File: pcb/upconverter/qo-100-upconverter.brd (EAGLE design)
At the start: 100 x 70 mm, 222 parts, among them CON1 3P-SH-SIDE, CON2 2EDG-2P-5MM-H, U1 EFM32TG11B120F128GM32, U10 LTC5597, U11 2450BP15E0100, U12 DC2337J5010AHF, U13 MCP6V31, U14 SKY66292-11, U15 F1958NBGK, U16 MCP9802-A0, U17 MCP1700-330, U18 LT8636, U19 MCP3421-A0, U2 DSB321SDA, U20 MCP6C02-020, U21 ADP7142AUJZ-3.3, U22 ADP7142AUJZ-3.3, U23 ADP7142AUJZ-3.3, U24 ADM7171ACPZ-5.0, U25 ADM7172ACPZ-5.0, U3 ADF4351, U4 F1958NBGK, U5 MAX2671, U6 2450BP15E0100, U7 F1958NBGK, U8 ADL5601, U9 F1490NLGA

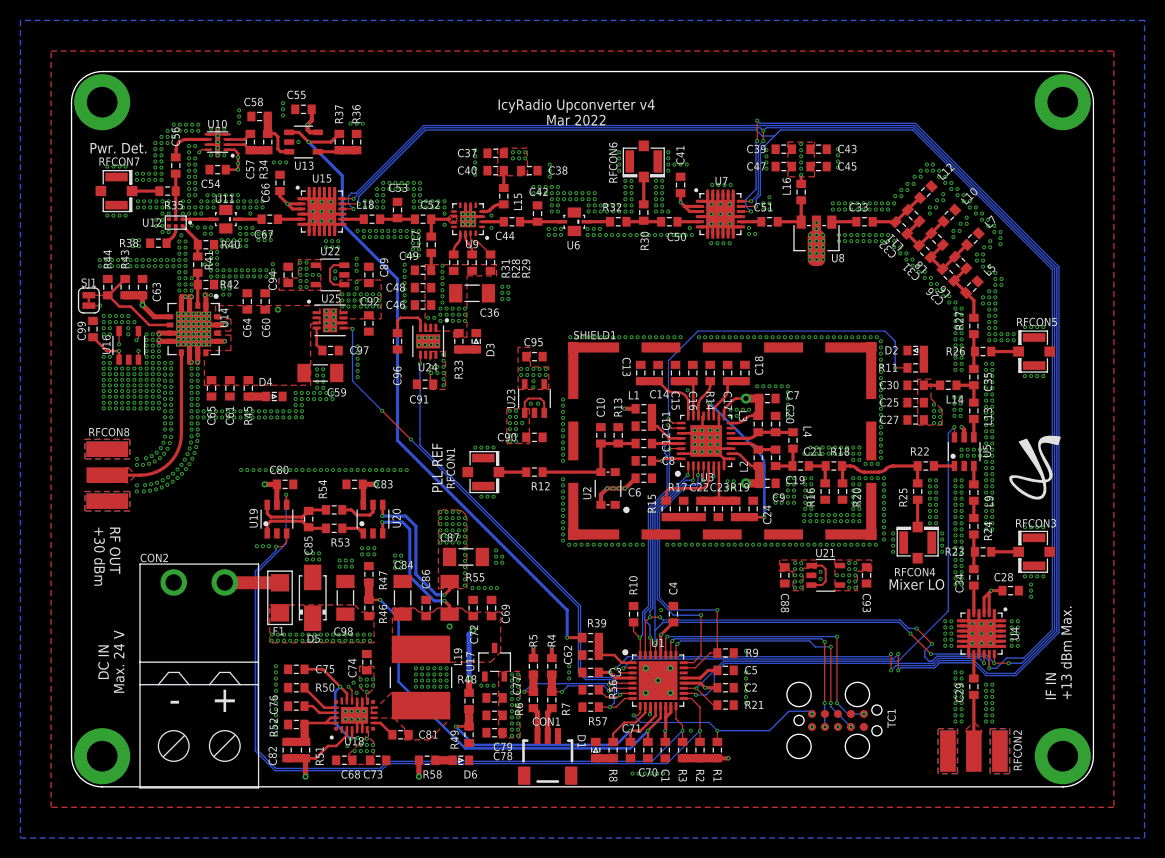
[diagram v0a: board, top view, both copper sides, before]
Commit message: Add RF switch
Signed-off-by: João Silva <jgc3silva@gmail.com>
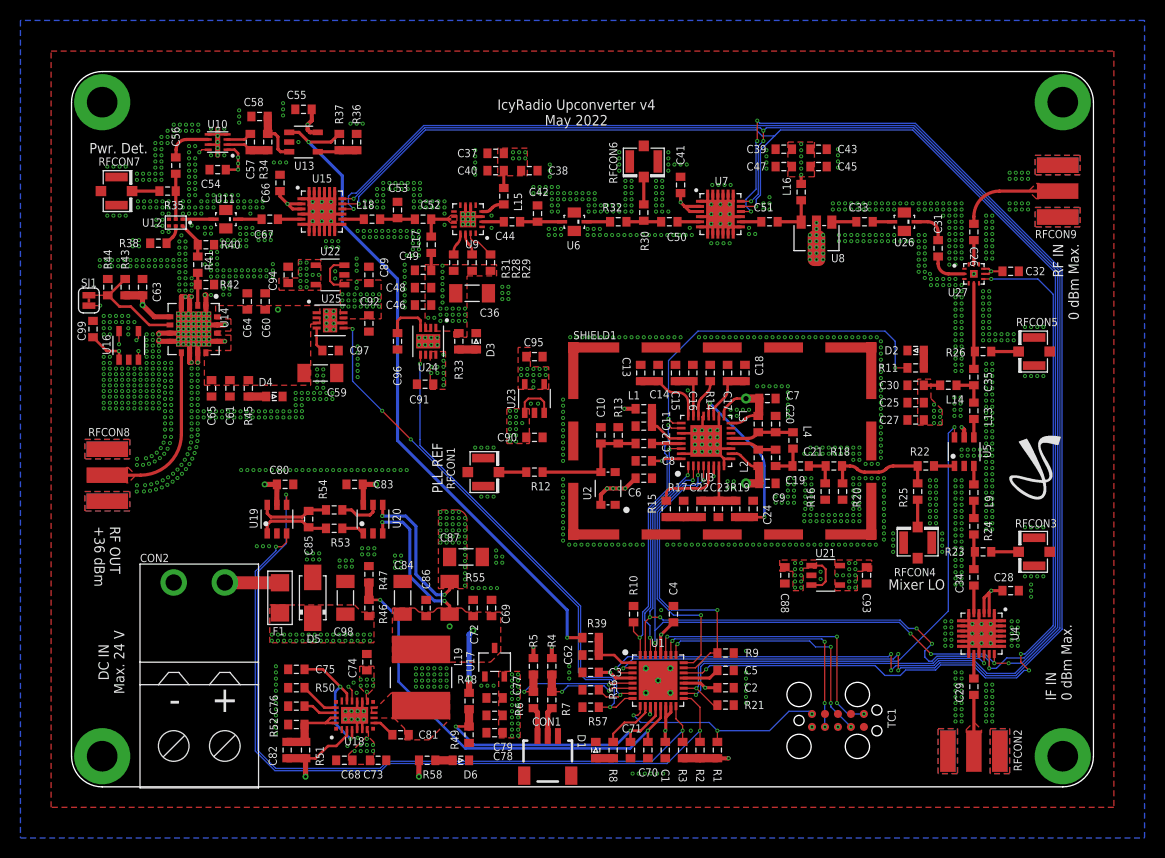
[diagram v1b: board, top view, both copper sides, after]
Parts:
- removed L10: 1.8pF, Inductor:IND0603
- removed L11, L8: 0 Ohms, Inductor:IND0603
- removed L12: 2.2pF, Inductor:IND0603
- removed L5, L6: 5.1nH, Inductor:IND0603
- removed L7: 3.3nH, Inductor:IND0603
- removed R27: 0 Ohms, Resistor:RES0603
- added RFCON9: RFCON-SMA-EDGE, RF Connector:SMA-EDGE
- added U26: 2450BP15E0100, Generic Filter:2450BP15E0100
- added U27: JSW2-63DR+, Mini Circuits:MT1818
- C26: value 1.2pF -> 12pF
- C31: value DNP -> 12pF
- C32: value DNP -> 100nF
- moved C32 11.5 mm to (91.9, 50.5), turned to 0 degrees
- moved C26 4.89 mm to (88.3, 54.3), turned to 270 degrees
- moved C31 1.33 mm to (84.8, 52.7), turned to 90 degrees
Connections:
- net RF_LOL_FLT_ACC renamed RF_FLT_ACC
- removed net 3V3_IF_ATT_MIXER_CLEAN: C25.1, C27.1, C28.1, C30.1, C93.1, L14.2, U21.4, U21.5, U4.2, U4.3, U5.5
- removed net MIXER_OUT_ACC_PROBE: C35.2, R26.1, R27.2
- removed net N$32: C26.2, C31.1, L6.2, L7.2, L8.1
- removed net N$33: C31.2, C32.1, L10.2, L11.1, L8.2
- removed net N$34: C32.2, C33.1, L11.2, L12.2
- removed net RF_ACC: C26.1, L5.2, L6.1, R27.1
- new net 3V3_IF_ATT_MIXER_SW_CLEAN: C25.1, C27.1, C28.1, C30.1, C32.1, C93.1, L14.2, U21.4, U21.5, U27.8, U27.9, U4.2, U4.3, U5.5
- new net MIXER_OUT_ACC: C35.2, R26.1, U27.5
- new net RF_IN_ACC: C26.2, U27.11
- new net RF_IN_DCC: C26.1, RFCON9.SIG
- new net RF_SEL_ACC: C31.2, U26.4
- new net RF_SEL_DCC: C31.1, U27.2
- new net RF_SEL_FILT_DCC: C33.1, U26.2
- new net RF_SW_CTL: U1.22, U27.7
- net GND: now also C32.2, RFCON9.GND@0, RFCON9.GND@1, RFCON9.GND@2, RFCON9.GND@3, U26.1, U26.3, U27.1, U27.10, U27.12, U27.17, U27.3, U27.4, U27.6; no longer L10.1, L12.1, L5.1, L7.1
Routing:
- net RF_SW_CTL: track 0.00 -> 81.9 mm, vias 0 -> 4
- net 3V3_IF_ATT_MIXER_SW_CLEAN: track 0.00 -> 11.4 mm, vias 0 -> 22
- net RF_IN_DCC: track 0.00 -> 9.94 mm
- net MIXER_OUT_ACC: track 0.00 -> 8.65 mm
- net 3V3_IF_ATT_MIXER_CLEAN: track 8.58 -> 0.00 mm, vias 21 -> 0
- net N$32: track 6.73 -> 0.00 mm
- net N$33: track 6.73 -> 0.00 mm
- net RF_ACC: track 6.22 -> 0.00 mm
- net N$34: track 5.63 -> 0.00 mm
- net RF_SEL_DCC: track 0.00 -> 3.69 mm
- net MIXER_OUT_ACC_PROBE: track 3.50 -> 0.00 mm
- net RF_SEL_ACC: track 0.00 -> 3.31 mm
- net RF_IN_ACC: track 0.00 -> 2.38 mm
- net RF_SEL_FILT_DCC: track 0.00 -> 1.90 mm
- net !MIXER_SHDN: track 51.2 -> 52.4 mm
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- added copper zone on layer 1, net 3V3_IF_ATT_MIXER_SW_CLEAN
- added copper zone on layer 15, net 3V3_IF_ATT_MIXER_SW_CLEAN
- added copper zone on layer 1, net RF_IN_DCC
- removed copper zone on layer 1, net 3V3_IF_ATT_MIXER_CLEAN
- removed copper zone on layer 15, net 3V3_IF_ATT_MIXER_CLEAN
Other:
- board text added: "IF IN 0 dBm Max."
- board text added: "IcyRadio Upconverter v4 May 2022"
- board text added: "RF IN 0 dBm Max."
- board text added: "RF OUT +36 dBm"
- board text removed: "IF IN +13 dBm Max."
- board text removed: "IcyRadio Upconverter v4 Mar 2022"
- board text removed: "RF OUT +30 dBm"

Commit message: Add Mixer and RF Switch indicator LEDs Slightly raise switched 5V0 rail voltage to account for larger current drawn from higher power last stage Remove dedicated ADC for current sampling Added PCB preview pictures Added schematic PDF
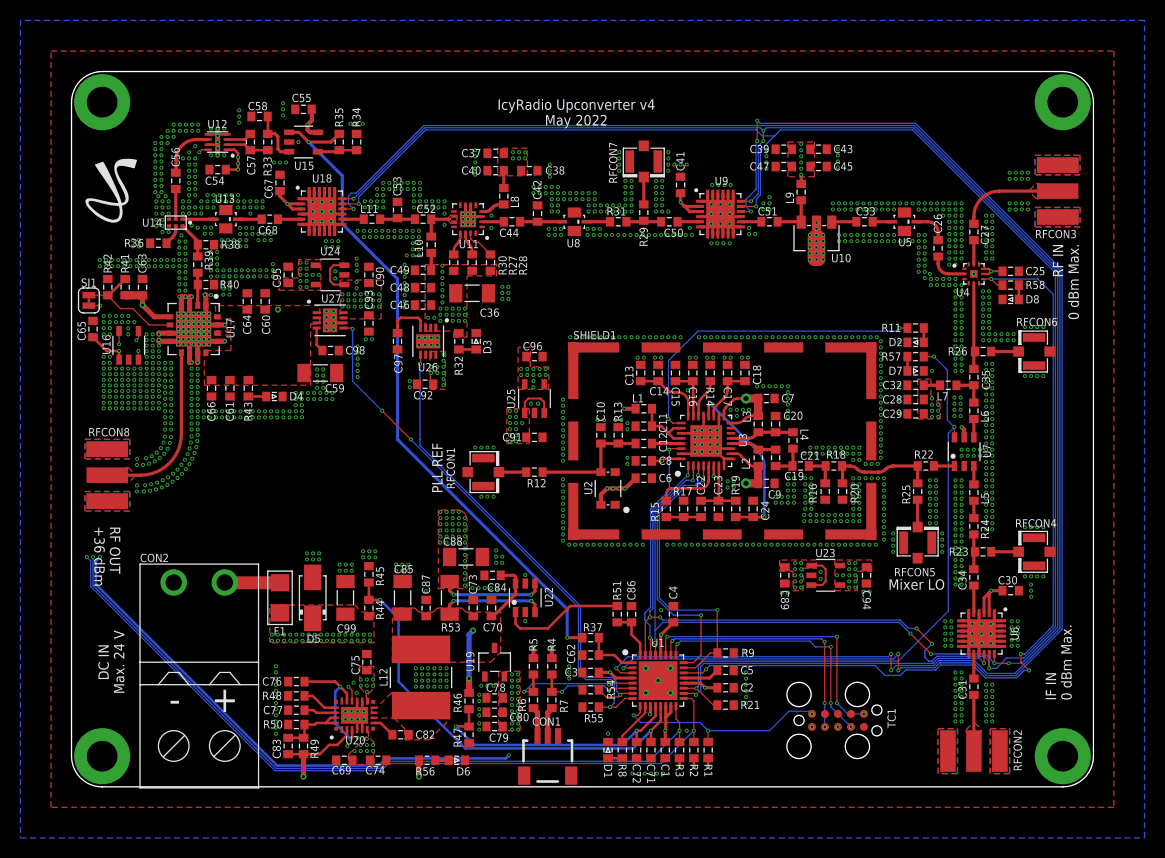
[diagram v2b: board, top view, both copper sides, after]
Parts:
- removed C81: 100nF, Capacitor:CAP0603
- removed L16: 470nH, Inductor:IND0603
- removed R10: 100K Ohms, Resistor:RES0603
- removed R52: 221K Ohms, Resistor:RES0603
- removed RFCON9: RFCON-SMA-EDGE, RF Connector:SMA-EDGE
- removed U21: ADP7142AUJZ-3.3, Analog Devices:SOT23-5
- added D7, D8: LED0603, LED:0603
- added L5: 18nH, Inductor:IND0603
- added R27: 1K Ohms, Resistor:RES0603
- C25: value 1uF -> 100nF
- C26, C33: value 12pF -> 15pF
- C27: value 100nF -> 15pF
- C28: value 100nF -> 1uF
- C29: value 100pF -> 100nF
- C30: value 47pF -> 100nF
- C31: value 12pF -> 100pF
- C32: value 100nF -> 47pF
- C65: value 10nF -> 100nF
- C66, C77: value 100nF -> 10nF
- C67: value 15pF -> 100nF
- C68: value 4.7uF -> 15pF
- C69: value 100nF -> 4.7uF
- C70: value 470pF -> 100nF
- C72: value 4.7uF -> 470pF
- C73: value 1uF -> 4.7uF
- C76: value 10nF -> 1uF
- C78: value 10uF -> 100nF
- C80: value 100nF -> 10uF
- C82: value 10pF -> 100nF
- C83: value 1uF -> 10pF
- C84: value 100uF -> 1uF; device Capacitor:CAP1206 -> Capacitor:CAP0603
- C85: value 100nF -> 100uF; device Capacitor:CAP0603 -> Capacitor:CAP1206
- C87: value 22uF -> 100nF; device Capacitor:CAP1206 -> Capacitor:CAP0603
- C88: value 1uF -> 22uF; device Capacitor:CAP0603 -> Capacitor:CAP1206
- C93: value 10uF -> 1uF
- C96: value 1nF -> 10uF
- C98: value 10uF -> 1nF; device Capacitor:CAP1206 -> Capacitor:CAP0603
- C99: value 100nF -> 10uF; device Capacitor:CAP0603 -> Capacitor:CAP1206
- L9: value 18nH -> 470nH
- R28: value 1K Ohms -> DNP
- R30: value DNP -> 1.5K Ohms
- R31: value 1.5K Ohms -> 0 Ohms
- R32: value 0 Ohms -> 510 Ohms
- R33: value 510 Ohms -> 0 Ohms
- R34: value 0 Ohms -> 1K Ohms
- R35: value DNP -> 2K Ohms
- R36: value 1K Ohms -> 49.9 Ohms
- R37: value 2K Ohms -> 100 Ohms
- R38: value 49.9 Ohms -> 96.1 Ohms
- R39: value 100 Ohms -> 71.5 Ohms
- R41: value 71.5 Ohms -> 10K Ohms
- R42: value 96.1 Ohms -> 7.5K Ohms
- R43: value 10K Ohms -> 510 Ohms
- R44: value 7.5K Ohms -> 100K Ohms
- R45: value 510 Ohms -> 10K Ohms
- R47: value 10K Ohms -> 75K Ohms
- R48: value 100K Ohms -> 41.2K Ohms
- R49: value 75K Ohms -> 1M Ohms
- R50: value 41.2K Ohms -> 220K Ohms
- R51: value 1M Ohms -> 1K Ohms
- R53: value 10K Ohms -> 0.03 Ohms; device Resistor:RES0603 -> Resistor:RES1206
- R54: value 10K Ohms -> 100K Ohms
- R55: value 0.03 Ohms -> 100K Ohms; device Resistor:RES1206 -> Resistor:RES0603
- R56: value 100K Ohms -> 1K Ohms
- R57: value 100K Ohms -> 330 Ohms
- R58: value 1K Ohms -> 330 Ohms
- RFCON3: value RFCON-U.FL -> RFCON-SMA-EDGE; device RF Connector:U.FL -> RF Connector:SMA-EDGE
- U10: value LTC5597 -> ADL5601; device Analog Devices:DFN8_2X2 -> Analog Devices:SOT89
- U11: value 2450BP15E0100 -> F1490NLGA; device Generic Filter:2450BP15E0100 -> Renesas:QFN16
- U12: value DC2337J5010AHF -> LTC5597; device Anaren:DC2337J5010AHF -> Analog Devices:DFN8_2X2
- U13: value MCP6V31 -> 2450BP15E0100; device Microchip:SOT23-5 -> Generic Filter:2450BP15E0100
- U14: value SKY66292-11 -> DC2337J5010AHF; device Skyworks:SKY66292-11 -> Anaren:DC2337J5010AHF
- U15: value F1958NBGK -> MCP6V31; device Renesas:QFN24_2 -> Microchip:SOT23-5
- U17: value MCP1700-330 -> SKY66292-11; device Microchip:SOT23 -> Skyworks:SKY66292-11
- U18: value LT8636 -> F1958NBGK; device Analog Devices:QFN20_ASYM_3X4_CORNER -> Renesas:QFN24_2
- U19: value MCP3421-A0 -> MCP1700-330; device Microchip:SOT23-6 -> Microchip:SOT23
- U20: value MCP6C02-020 -> LT8636; device Microchip:SOT23-6 -> Analog Devices:QFN20_ASYM_3X4_CORNER
- U22: value ADP7142AUJZ-3.3 -> MCP6C02-020; device Analog Devices:SOT23-5 -> Microchip:SOT23-6
- U24: value ADM7171ACPZ-5.0 -> ADP7142AUJZ-3.3; device Analog Devices:LFCSP8_3X3 -> Analog Devices:SOT23-5
- U25: value ADM7172ACPZ-5.0 -> ADP7142AUJZ-3.3; device Analog Devices:LFCSP8_3X3 -> Analog Devices:SOT23-5
- U26: value 2450BP15E0100 -> ADM7171ACPZ-5.0; device Generic Filter:2450BP15E0100 -> Analog Devices:LFCSP8_3X3
- U27: value JSW2-63DR+ -> ADM7172ACPZ-5.0; device Mini Circuits:MT1818 -> Analog Devices:LFCSP8_3X3
- U4: value F1958NBGK -> JSW2-63DR+; device Renesas:QFN24_2 -> Mini Circuits:MT1818
- U5: value MAX2671 -> 2450BP15E0100; device Maxim Integrated:SOT23-6 -> Generic Filter:2450BP15E0100
- U6: value 2450BP15E0100 -> F1958NBGK; device Generic Filter:2450BP15E0100 -> Renesas:QFN24_2
- U7: value F1958NBGK -> MAX2671; device Renesas:QFN24_2 -> Maxim Integrated:SOT23-6
- U8: value ADL5601 -> 2450BP15E0100; device Analog Devices:SOT89 -> Generic Filter:2450BP15E0100
- U9: value F1490NLGA -> F1958NBGK; device Renesas:QFN16 -> Renesas:QFN24_2
- moved LOGO1 94.4 mm to (6.60, 61.6)
- moved R58 73.6 mm to (91.9, 49.1)
- moved C94 63.8 mm to (77.8, 20.7), turned to 270 degrees
- moved U27 63.2 mm to (25.3, 45.6)
- moved U10 59.3 mm to (72.9, 53.7)
- moved U6 56.7 mm to (89.0, 15.0), turned to 270 degrees
- moved C93 54.6 mm to (29.1, 45.4)
- moved R37 54.4 mm to (50.8, 14.6), turned to 180 degrees
- moved C68 53.5 mm to (19.4, 55.5)
- moved R39 53.0 mm to (12.3, 51.1), turned to 90 degrees
- moved RFCON7 51.7 mm to (56.0, 61.2), turned to 270 degrees
- moved C89 50.2 mm to (69.8, 20.7), turned to 270 degrees
- moved U18 49.4 mm to (24.5, 56.3), turned to 0 degrees
- moved U26 48.0 mm to (34.9, 43.6), turned to 270 degrees
- moved R57 46.8 mm to (82.6, 42.1)
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- renumbered L13 to L6, L14 to L7, L15 to L8, L17 to L10, L18 to L11, L19 to L12
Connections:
- removed net !PLL_MUTE: R10.2, U1.32, U3.26
- removed net 5V0_ISENSE_VN: C85.2, R54.1, U19.6
- removed net 5V0_ISENSE_VP: C85.1, R53.1, U19.1
- removed net N$10: R53.2, U20.1
- removed net N$48: R35.2, RFCON7.P$3
- new net N$5: D7.A, R57.1
- new net N$9: D8.A, R58.1
- new net V5V0_ISENSE: C86.1, R51.1, U1.32
- new net V5V0_ISENSE-AMP: R51.2, U22.1
- net !MIXER_SHDN: now also R57.2, U7.6; no longer U5.6
- net 3V3: now also C65.1, U19.2; no longer C77.1, C99.1, U17.2, U19.5
- net 3V3_IF_ATT_MIXER_SW_CLEAN: now also C29.1, C94.1, U23.4, U23.5, U4.8, U4.9, U6.2, U6.3, U7.5; no longer C27.1, C93.1, U21.4, U21.5, U27.8, U27.9, U4.2, U4.3, U5.5
- net 3V3_PLL_CLEAN: now also C96.1, U25.4, U25.5; no longer C95.1, U23.4, U23.5
- net 3V3_RF_ATT_PDET_CLEAN: now also C67.1, C95.1, U12.1, U12.8, U15.5, U18.2, U18.3, U24.4, U24.5, U9.2, U9.3; no longer C66.1, C94.1, U10.1, U10.8, U13.5, U15.2, U15.3, U22.4, U22.5, U7.2, U7.3
- net 5V0: now also C70.1, C73.1, C85.1, C87.1, R46.2, R49.2, R53.2, R56.2, U19.3, U20.2, U22.3, U22.6; no longer C69.1, C72.1, C82.1, C86.1, R48.2, R51.2, R55.2, R58.2, U17.3, U18.2, U20.3, U20.6
- net 5V0_BST: now also C82.2, U20.7; no longer C81.2, U18.7
- net 5V0_FB: now also C83.2, R49.1, R50.2, U20.19, U20.20; no longer C82.2, R51.1, R52.2, U18.19, U18.20
- net 5V0_INTVCC: now also C76.1, U20.15, U20.3; no longer C75.1, U18.15, U18.3
- net 5V0_ISENSE: now also C93.1, R53.1, U22.4, U24.1, U24.3, U25.1, U25.3, U26.7, U26.8, U27.7, U27.8; no longer C87.1, R55.1, U20.4, U21.1, U21.3, U22.1, U22.3, U24.7, U24.8, U25.7, U25.8
- net 5V0_PA_STG1_2_CLEAN: now also L9.2, R27.2, R30.2, R32.2, U26.1, U26.2, U26.3; no longer L16.2, R29.2, R31.2, R33.2, U24.1, U24.2, U24.3
- net 5V0_PA_STG3_CLEAN: now also C66.1, R41.2, U17.12, U17.14, U17.16, U17.5, U27.1, U27.2, U27.3; no longer C65.1, R45.2, U14.12, U14.14, U14.16, U14.5, U25.1, U25.2, U25.3
- net 5V0_RT: now also R48.2, U20.17; no longer R50.2, U18.17
- net 5V0_SS: now also C77.1, U20.18; no longer C76.1, U18.18
- net 5V0_SW: now also C82.1, U20.10, U20.8, U20.9; no longer C81.1, U18.10, U18.8, U18.9
- net 5V0_VSENSE: now also C72.1, R46.1, R47.2; no longer C71.1, R48.1, R49.2
- net GND: now also C29.2, C67.2, C85.2, D7.C, D8.C, R34.1, R45.1, R48.1, R54.1, R55.1, RFCON3.GND@0, RFCON3.GND@1, RFCON3.GND@2, RFCON3.GND@3, U10.2, U11.12, U11.17, U11.5, U11.6, U11.7, U11.8, U11.9, U12.5, U12.7, U12.9, U13.1, U13.3, U15.2, U17.10, U17.11, U17.13, U17.15, U17.17, U17.3, U17.4, U17.7, U17.8, U18.1, U18.10, U18.11, U18.15, U18.19, U18.20, U18.22, U18.23, U18.24, U18.25, U18.6, U18.7, U18.8, U18.9, U19.1, U20.12, U20.13, U20.21, U20.4, U20.M1, U20.M2, U20.M3, U20.M4, U22.5, U24.2, U25.2, U26.6, U26.9, U27.9, U4.17, U4.3, U5.1, U5.3, U6.10, U6.11, U6.12, U6.13, U6.15, U6.19, U6.20, U6.21, U6.22, U6.23, U6.24, U6.25, U6.4, U6.6, U6.7, U6.8, U6.9, U7.2, U8.1, U8.3, U9.10, U9.11, U9.13, U9.15, U9.19, U9.20, U9.21, U9.22, U9.23, U9.24, U9.25, U9.4; no longer C27.2, C68.2, C83.2, R10.1, R44.1, R49.1, R52.1, R54.2, R56.1, R57.1, RFCON3.P$1, RFCON3.P$2, RFCON9.GND@0, RFCON9.GND@1, RFCON9.GND@2, RFCON9.GND@3, U10.5, U10.7, U10.9, U12.3, U13.2, U14.1, U14.10, U14.11, U14.13, U14.15, U14.17, U14.7, U14.8, U15.1, U15.10, U15.11, U15.12, U15.13, U15.15, U15.19, U15.20, U15.21, U15.22, U15.23, U15.24, U15.25, U15.4, U15.6, U15.7, U15.8, U15.9, U18.5, U18.M1, U18.M2, U18.M3, U18.M4, U19.2, U20.2, U21.2, U24.6, U24.9, U25.6, U25.9, U26.1, U26.3, U27.1, U27.10, U27.12, U27.17, U27.3, U27.4, U4.11, U4.13, U4.15, U4.19, U4.20, U4.21, U4.22, U4.23, U4.24, U4.25, U4.7, U4.8, U4.9, U5.2, U6.3, U7.1, U7.10, U7.11, U7.12, U7.13, U7.15, U7.19, U7.20, U7.21, U7.22, U7.23, U7.24, U7.25, U7.4, U7.6, U7.7, U7.8, U7.9, U8.2, U8.4, U9.17, U9.3, U9.5
- net I2C1_SCL: no longer U19.3
- net I2C1_SDA: no longer U19.4
- net IF_ATT_ACC: now also L5.1; no longer L9.1
- net IF_ATT_DCC: now also U6.5; no longer U4.5
- net IF_ATT_LE: now also U6.16; no longer U4.16
- net IF_IN_ACC: now also C31.2, U6.14; no longer C29.2, U4.14
- net IF_IN_DCC: now also C31.1; no longer C29.1
- net MIXER_IN_DCC: now also L5.2, U7.3; no longer L9.2, U5.3
- net MIXER_OUT_ACC: now also U4.5; no longer U27.5
- net MIXER_OUT_DCC: now also U7.4; no longer U5.4
- net N$12: now also U11.4; no longer U9.4
- net N$149: now also R56.1; no longer R58.1
- net N$15: now also R27.1, U11.14; no longer R28.1, U9.14
- net N$16: now also R30.1, U11.13; no longer R31.1, U9.13
- net N$2: now also C98.1, U27.4; no longer C97.1, U25.4
- net N$20: now also C97.1, U26.4; no longer C96.1, U24.4
- net N$23: now also R32.1; no longer R33.1
- net N$24: now also RFCON4.P$3; no longer RFCON3.P$3
- net N$28: now also RFCON6.P$3; no longer RFCON5.P$3
- net N$3: now also R43.1; no longer R45.1
- net N$30: now also U11.2; no longer U9.2
- net N$35: now also R29.2, RFCON7.P$3; no longer R30.2, RFCON6.P$3
- net N$39: now also U18.14; no longer U15.14
- net N$4: now also R28.1, U11.15; no longer R29.1, U9.15
- net N$42: now also R36.2, U14.5; no longer R38.2, U12.5
- net N$43: now also U12.6; no longer U10.6
- net N$44: now also U12.3; no longer U10.3
- net N$45: now also U7.1; no longer U5.1
- net N$47: now also RFCON5.P$3; no longer RFCON4.P$3
- net N$7: now also R34.2, R35.2, U15.4; no longer R36.2, R37.2, U13.4
- net N$8: now also U3.26
- net PA3_EN: now also R41.1, R42.2, U17.6; no longer R43.1, R44.2, U14.6
- net PA_STG1_2_BIAS_EN: now also R54.2, U26.5; no longer R56.2, U24.5
- net PA_STG3_BIAS_EN: now also R55.2, U27.5; no longer R57.2, U25.5
- net RF_ATT1_LE: now also U9.16; no longer U7.16
- net RF_ATT2_LE: now also U18.16; no longer U15.16
- net RF_FINAL_ACC: now also U17.9; no longer U14.9
- net RF_FLT_ACC: now also U10.1; no longer U8.1
- net RF_IN_ACC: now also C27.2, U4.11; no longer C26.2, U27.11
- net RF_IN_DCC: now also C27.1, RFCON3.SIG; no longer C26.1, RFCON9.SIG
- net RF_PRE1_ACC: now also U9.14; no longer U7.14
- net RF_PRE1_ATT_ACC: now also R31.1, U8.4; no longer R32.1, U6.4
- net RF_PRE1_ATT_ACC_PROBE: now also R29.1, R31.2; no longer R30.1, R32.2
- net RF_PRE1_ATT_DCC: now also U9.5; no longer U7.5
- net RF_PRE1_ATT_FLT_ACC: now also U8.2; no longer U6.2
- net RF_PRE1_DCC: now also L9.1, U10.3; no longer L16.1, U8.3
- net RF_PRE2_ATT_ACC: now also C68.2, U13.4; no longer C67.2, U11.4
- net RF_PRE2_ATT_DCC: now also C68.1, U18.5; no longer C67.1, U15.5
- net RF_PRE2_ATT_FLT_ACC: now also U13.2, U14.1; no longer U11.2, U12.1
- net RF_PRE2_ATT_FLT_CPL_ACC: now also U14.2; no longer R35.1, U12.2
- net RF_PRE2_ATT_FLT_THRU_ACC: now also R38.2, R39.2, U14.6; no longer R40.2, R41.2, U12.6
- net RF_PRE2_ATT_FLT_THRU_ACC_ATT: now also R39.1, R40.2, U17.2; no longer R41.1, R42.2, U14.2
- net RF_PRE2_DCC: now also U11.10, U11.11; no longer U9.10, U9.11
- net RF_SEL_ACC: now also C26.2, U5.4; no longer C31.2, U26.4
- net RF_SEL_DCC: now also C26.1, U4.2; no longer C31.1, U27.2
- net RF_SEL_FILT_DCC: now also U5.2; no longer U26.2
- net RF_SW_CTL: now also R58.2, U4.7; no longer U27.7
- net SPI_MOSI: now also U18.18, U6.18, U9.18; no longer U15.18, U4.18, U7.18
- net SPI_SCK: now also U18.17, U6.17, U9.17; no longer U15.17, U4.17, U7.17
- net VIN: now also C69.1, C75.1, C99.1, R44.2, U20.11, U20.14, U20.6; no longer C68.1, C73.1, C98.1, R46.2, U18.11, U18.14, U18.6
- net VIN_VSENSE: now also C71.1, R44.1, R45.2; no longer C70.1, R46.1, R47.2
- net VPDET_AMP: now also R35.1, R37.2, U15.1; no longer R37.1, R39.2, U13.1
- net VPDET_FLT: now also R33.1, U15.3; no longer R34.1, U13.3
- net VPDET_RAW: now also R33.2, U12.2; no longer R34.2, U10.2
- net VPDET_SENSE: now also R37.1; no longer R39.1
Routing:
- net !PLL_MUTE: track 27.0 -> 0.00 mm, vias 2 -> 0
- net 5V0: track 74.6 -> 56.2 mm, vias 8 -> 6
- net I2C1_SDA: track 112.9 -> 96.8 mm
- net I2C1_SCL: track 116.9 -> 102.3 mm
- net V5V0_ISENSE-AMP: track 0.00 -> 12.2 mm
- net !MIXER_SHDN: track 52.4 -> 61.1 mm, vias 2 -> 3
- net 5V0_ISENSE_VN: track 7.04 -> 0.00 mm
- net 5V0_ISENSE_VP: track 7.04 -> 0.00 mm
- net V5V0_ISENSE: track 0.00 -> 4.95 mm
- net 5V0_ISENSE: track 27.5 -> 23.2 mm
- net GND: track 155.3 -> 151.3 mm, vias 1722 -> 1718
- net PLL_LOCK: track 34.7 -> 31.8 mm
- net N$48: track 2.67 -> 0.00 mm
- net N$10: track 2.26 -> 0.00 mm
- net RF_PRE2_ATT_FLT_CPL_ACC: track 4.49 -> 2.97 mm
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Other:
- board text removed: "Pwr. Det."
